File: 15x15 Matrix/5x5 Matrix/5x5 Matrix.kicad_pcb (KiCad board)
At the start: 2 copper layers, 111 parts, among them J1 Conn_01x02, SW1 SWP, SW10 SWP, SW11 SWP, SW12 SWP, SW13 SWP, SW14 SWP, SW15 SWP, SW16 SWP, SW17 SWP, SW18 SWP, SW19 SWP, SW2 SWP, SW20 SWP, SW21 SWP, SW22 SWP, SW23 SWP, SW24 SWP, SW25 SWP, SW3 SWP, SW4 SWP, SW5 SWP, SW6 SWP, SW7 SWP, SW8 SWP, SW9 SWP, U1 MCP23017-E/SO, U2 74AHCT1G125

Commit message: Added more pcb stuff
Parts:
- C1, C10, C11, C12, C13, C14, C15, C16, C17, C18, C19, C2, C20, C21, C22, C23, C24, C25, C27, C3, C4, C5, C6, C7, C8, C9, CPI1, CPI2, D26, D27, D28, D29, D30, D31, D32, D33, D34, D35, D36, D37, D38, D39, D40, D41, D42, D43, D44, D45, D46, D47, D48, D49, D50: moved to B.Cu
- moved D30 138.5 mm to (103.7, 40.1), turned to 180 degrees
- moved D31 126.4 mm to (103.7, 59.1), turned to 180 degrees
- moved D29 125.5 mm to (84.6, 40.1), turned to 180 degrees
- moved D28 114.4 mm to (65.6, 40.1), turned to 180 degrees
- moved D27 105.7 mm to (46.5, 40.1), turned to 180 degrees
- moved C1 102.0 mm to (27.6, 43.2), turned to 180 degrees
- moved D26 100.2 mm to (27.5, 40.1), turned to 180 degrees
- moved D48 31.0 mm to (24.9, 144.7), turned to 180 degrees
- moved D49 31.0 mm to (24.9, 149.3), turned to 180 degrees
- moved D50 31.0 mm to (24.9, 153.8), turned to 180 degrees
- moved D32 17.7 mm to (49.2, 167.5), turned to 180 degrees
- moved C25 17.2 mm to (60.6, 150.1), turned to 180 degrees
- moved CPI1 17.2 mm to (60.6, 155.4), turned to 180 degrees
- moved CPI2 17.2 mm to (60.6, 158.1), turned to 180 degrees
- moved C27 17.2 mm to (60.6, 152.7), turned to 180 degrees
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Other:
- board outline added: 3.2 x 2.8 mm

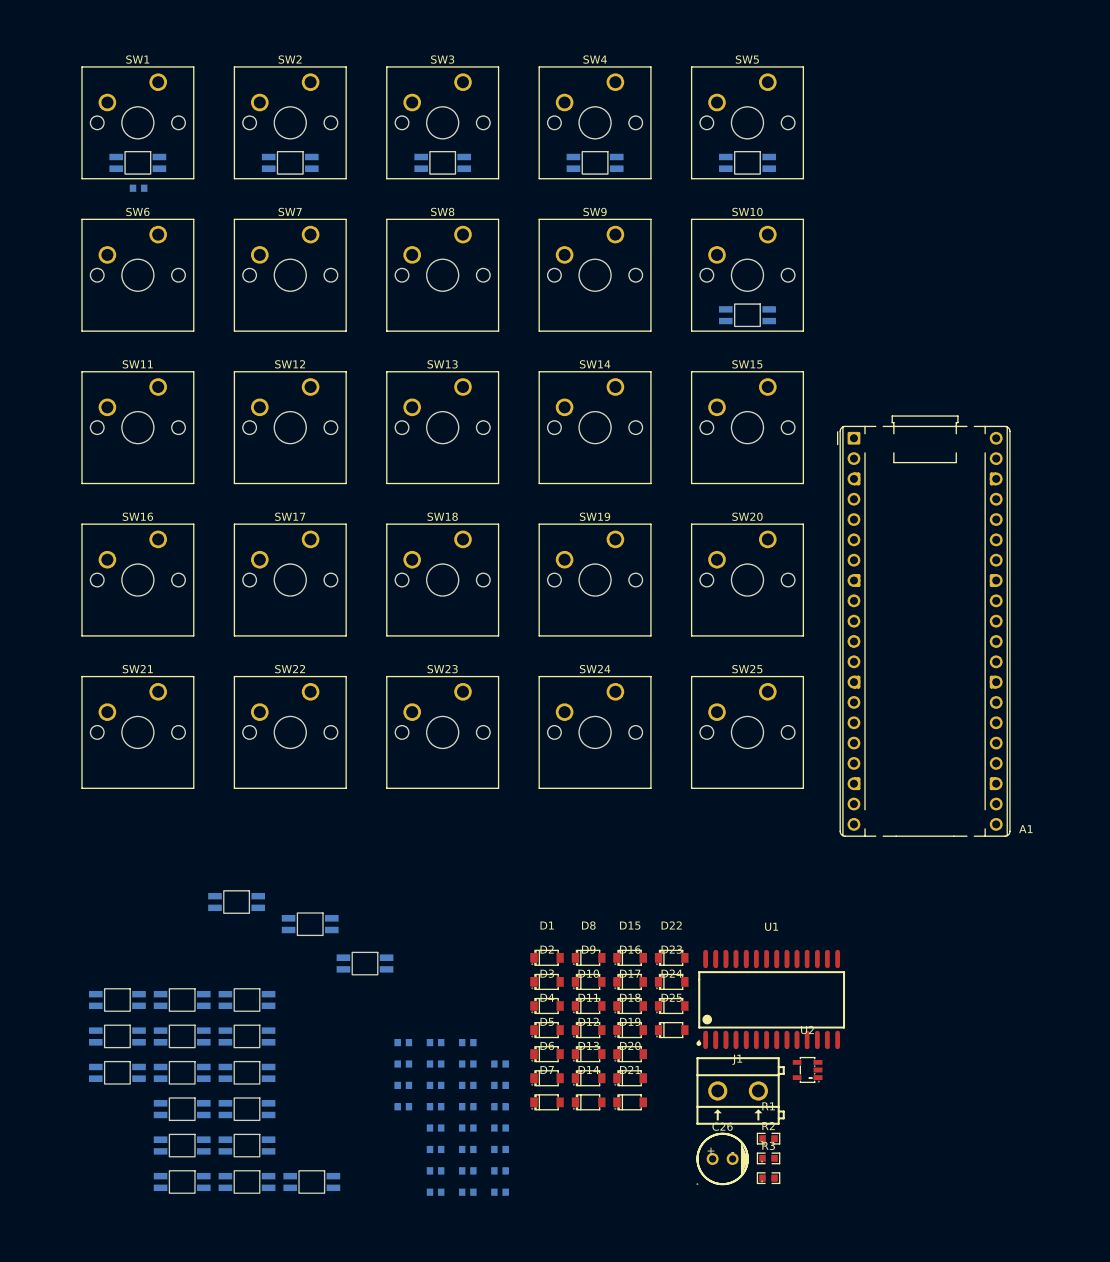
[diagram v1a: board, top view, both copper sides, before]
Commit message: Added led footprints
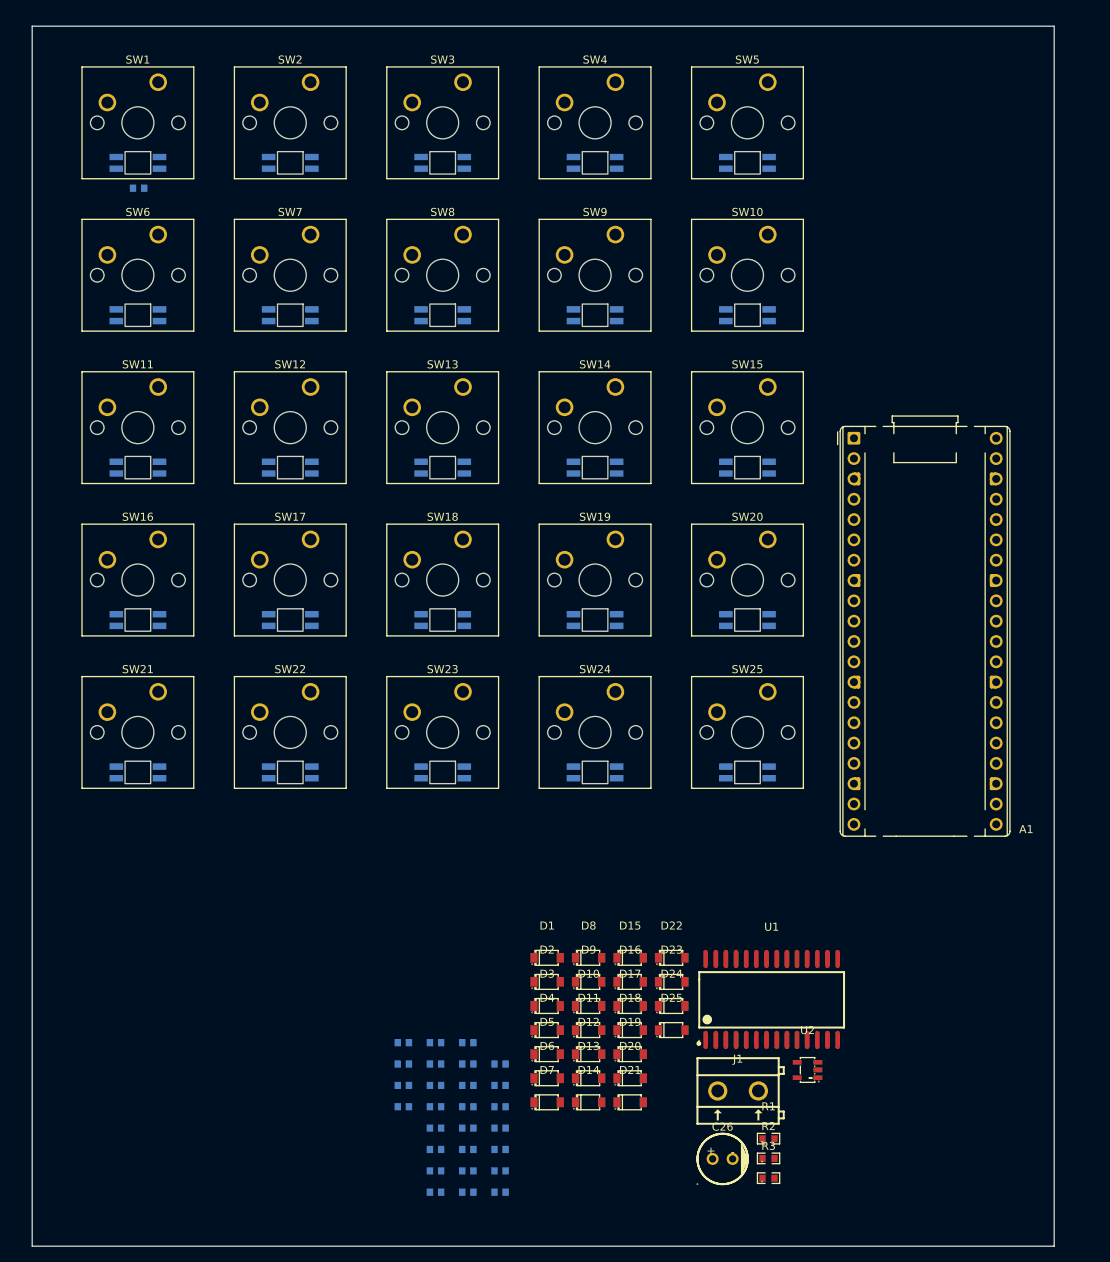
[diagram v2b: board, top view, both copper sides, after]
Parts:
- moved D32 114.0 mm to (84.6, 59.1)
- moved D39 99.3 mm to (84.6, 78.2)
- moved D35 91.2 mm to (27.5, 59.1)
- moved D38 88.2 mm to (65.6, 78.2)
- moved D50 87.3 mm to (103.7, 116.3)
- moved D34 85.8 mm to (46.5, 59.1)
- moved D41 85.1 mm to (103.7, 97.2)
- moved D37 80.4 mm to (46.5, 78.2)
- moved D40 79.0 mm to (103.7, 78.2)
- moved D33 77.7 mm to (65.6, 59.1)
- moved D36 76.9 mm to (27.5, 78.2)
- moved D42 73.3 mm to (84.6, 97.2)
- moved D49 68.2 mm to (84.6, 116.3)
- moved D45 65.9 mm to (27.5, 97.2)
- moved D43 65.3 mm to (65.6, 97.2)
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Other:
- board size 3.2 x 2.8 mm -> 127.8 x 152.5 mm
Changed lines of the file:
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@@
 	(footprint "footprints:C5149201_LED-SMD_4P-L3_2-W2_8-LS5_9_SK6812MINI-E"
 		(layer "B.Cu")
-		(at 33 167.475 180)
+		(at 27.46 116.28 180)
 		(property "Reference" "D46"
 			(at 0 4.725 0)
@@
 	(footprint "footprints:C5149201_LED-SMD_4P-L3_2-W2_8-LS5_9_SK6812MINI-E"
 		(layer "B.Cu")
-		(at 41.1 149.275 180)
+		(at 27.46 59.13 180)
 		(property "Reference" "D35"
 			(at 0 4.725 0)
@@
 	(footprint "footprints:C5149201_LED-SMD_4P-L3_2-W2_8-LS5_9_SK6812MINI-E"
 		(layer "B.Cu")
-		(at 24.9 153.825 180)
+		(at 103.66 116.28 180)
 		(property "Reference" "D50"
 			(at 0 4.725 0)
@@
 	(footprint "footprints:C5149201_LED-SMD_4P-L3_2-W2_8-LS5_9_SK6812MINI-E"
 		(layer "B.Cu")
-		(at 33 153.825 180)
+		(at 65.56 97.23 180)
 		(property "Reference" "D43"
 			(at 0 4.725 0)
@@
 	(footprint "footprints:C5149201_LED-SMD_4P-L3_2-W2_8-LS5_9_SK6812MINI-E"
 		(layer "B.Cu")
-		(at 33 158.375 180)
+		(at 46.51 97.23 180)
 		(property "Reference" "D44"
 			(at 0 4.725 0)
@@
 	(footprint "footprints:C5149201_LED-SMD_4P-L3_2-W2_8-LS5_9_SK6812MINI-E"
 		(layer "B.Cu")
-		(at 49.2 167.475 180)
+		(at 84.61 59.13 180)
 		(property "Reference" "D32"
 			(at 0 4.725 0)
@@
 	(footprint "footprints:C5149201_LED-SMD_4P-L3_2-W2_8-LS5_9_SK6812MINI-E"
 		(layer "B.Cu")
-		(at 39.8 132.48 180)
+		(at 65.56 59.13 180)
 		(property "Reference" "D33"
 			(at 0 4.725 0)
@@
 	(footprint "footprints:C5149201_LED-SMD_4P-L3_2-W2_8-LS5_9_SK6812MINI-E"
 		(layer "B.Cu")
-		(at 41.1 153.825 180)
+		(at 27.46 78.18 180)
 		(property "Reference" "D36"
 			(at 0 4.725 0)
@@
 	(footprint "footprints:C5149201_LED-SMD_4P-L3_2-W2_8-LS5_9_SK6812MINI-E"
 		(layer "B.Cu")
-		(at 33 149.275 180)
+		(at 84.61 97.23 180)
 		(property "Reference" "D42"
 			(at 0 4.725 0)
@@
 	(footprint "footprints:C5149201_LED-SMD_4P-L3_2-W2_8-LS5_9_SK6812MINI-E"
 		(layer "B.Cu")
-		(at 49 135.25 180)
+		(at 103.66 78.18 180)
 		(property "Reference" "D40"
 			(at 0 4.725 0)
@@
 	(footprint "footprints:C5149201_LED-SMD_4P-L3_2-W2_8-LS5_9_SK6812MINI-E"
 		(layer "B.Cu")
-		(at 41.1 144.725 180)
+		(at 46.51 59.13 180)
 		(property "Reference" "D34"
 			(at 0 4.725 0)
@@
 	(footprint "footprints:C5149201_LED-SMD_4P-L3_2-W2_8-LS5_9_SK6812MINI-E"
 		(layer "B.Cu")
-		(at 24.9 149.275 180)
+		(at 84.61 116.28 180)
 		(property "Reference" "D49"
 			(at 0 4.725 0)
@@
 	(footprint "footprints:C5149201_LED-SMD_4P-L3_2-W2_8-LS5_9_SK6812MINI-E"
 		(layer "B.Cu")
-		(at 41.1 158.375 180)
+		(at 46.51 78.18 180)
 		(property "Reference" "D37"
 			(at 0 4.725 0)
@@
 	(footprint "footprints:C5149201_LED-SMD_4P-L3_2-W2_8-LS5_9_SK6812MINI-E"
 		(layer "B.Cu")
-		(at 41.1 162.925 180)
+		(at 65.56 78.18 180)
 		(property "Reference" "D38"
 			(at 0 4.725 0)
@@
 	(footprint "footprints:C5149201_LED-SMD_4P-L3_2-W2_8-LS5_9_SK6812MINI-E"
 		(layer "B.Cu")
-		(at 33 162.925 180)
+		(at 27.46 97.23 180)
 		(property "Reference" "D45"
 			(at 0 4.725 0)
@@
 	(footprint "footprints:C5149201_LED-SMD_4P-L3_2-W2_8-LS5_9_SK6812MINI-E"
 		(layer "B.Cu")
-		(at 41.1 167.475 180)
+		(at 84.61 78.18 180)
 		(property "Reference" "D39"
 			(at 0 4.725 0)
@@
 	(footprint "footprints:C5149201_LED-SMD_4P-L3_2-W2_8-LS5_9_SK6812MINI-E"
 		(layer "B.Cu")
-		(at 33 144.725 180)
+		(at 103.66 97.23 180)
 		(property "Reference" "D41"
 			(at 0 4.725 0)
@@
 	(footprint "footprints:C5149201_LED-SMD_4P-L3_2-W2_8-LS5_9_SK6812MINI-E"
 		(layer "B.Cu")
-		(at 55.85 140.175 180)
+		(at 46.51 116.28 180)
 		(property "Reference" "D47"
 			(at 0 4.725 0)
@@
 	(footprint "footprints:C5149201_LED-SMD_4P-L3_2-W2_8-LS5_9_SK6812MINI-E"
 		(layer "B.Cu")
-		(at 24.9 144.725 180)
+		(at 65.56 116.28 180)
 		(property "Reference" "D48"
 			(at 0 4.725 0)
@@
 		)
 	)
+	(gr_rect
+		(start 14.25 23)
+		(end 142 175.5)
+		(stroke
+			(width 0.05)
+			(type default)
+		)
+		(fill no)
+		(layer "Edge.Cuts")
+	)
 	(embedded_fonts no)

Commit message: Fixed rotation of leds on pcb
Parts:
- turned D26 to 0 degrees
- turned D27 to 0 degrees
- turned D28 to 0 degrees
- turned D29 to 0 degrees
- turned D30 to 0 degrees
- turned D36 to 0 degrees
- turned D37 to 0 degrees
- turned D38 to 0 degrees
- turned D39 to 0 degrees
- turned D40 to 0 degrees
- turned D46 to 0 degrees
- turned D47 to 0 degrees
- turned D48 to 0 degrees
- turned D49 to 0 degrees
- turned D50 to 0 degrees

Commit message: 5x5 Ready for 1 sided printing
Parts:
- removed CPI1: 100nF, footprints:C14663_C0603
- C26: footprint footprints:C49304896_CAP-TH_BD6_3-P2_50-D0_5-FD -> Capacitor_THT:CP_Radial_D6.3mm_P2.50mm; moved to B.Cu
- D1, D10, D11, D12, D13, D14, D15, D16, D17, D18, D19, D2, D20, D21, D22, D23, D24, D25, D3, D4, D5, D6, D7, D8, D9, J1, R1, R2, R3, U1, U2: moved to B.Cu
- D26, D27, D28, D29, D30, D31, D32, D33, D34, D35, D36, D37, D38, D39, D40, D41, D42, D43, D44, D45, D46, D47, D48, D49, D50: footprint footprints:C5149201_LED-SMD_4P-L3_2-W2_8-LS5_9_SK6812MINI-E -> LED_SMD:LED_SK6812MINI-E_3.2x2.8mm_P1.5mm_ReverseMount
- moved R3 150.1 mm to (21.8, 43.0), turned to 180 degrees
- moved U2 145.0 mm to (15.8, 44.2), turned to 180 degrees
- moved D5 128.4 mm to (109.0, 26.8), turned to 180 degrees
- moved D4 122.3 mm to (89.9, 26.8), turned to 180 degrees
- moved D1 121.7 mm to (32.8, 26.8), turned to 180 degrees
- moved C5 121.7 mm to (103.7, 43.1)
- moved D3 119.0 mm to (70.8, 26.8), turned to 180 degrees
- moved D2 118.8 mm to (51.8, 26.8), turned to 180 degrees
- moved D6 118.0 mm to (32.8, 45.8), turned to 180 degrees
- moved C4 115.6 mm to (84.6, 43.1)
- moved D7 114.9 mm to (51.8, 45.8), turned to 180 degrees
- moved C27 114.5 mm to (15.4, 47.5), turned to 0 degrees
- moved C2 112.7 mm to (46.5, 43.1)
- moved C3 112.5 mm to (65.6, 43.1)
- moved C8 106.9 mm to (65.6, 62.1)
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- renumbered CPI2 to C28
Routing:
- net /5V: track 0.00 -> 727.9 mm
- net /ROW0: track 0.00 -> 260.6 mm, vias 0 -> 1
- net /3V3: track 0.00 -> 259.1 mm, vias 0 -> 3
- net /ROW1: track 0.00 -> 236.7 mm, vias 0 -> 1
- net /ROW2: track 0.00 -> 212.9 mm, vias 0 -> 1
- net /I2C_SDA: track 0.00 -> 205.6 mm, vias 0 -> 1
- net /I2C_SCL: track 0.00 -> 199.6 mm, vias 0 -> 1
- net /ROW3: track 0.00 -> 189.1 mm, vias 0 -> 1
- net /ROW4: track 0.00 -> 156.5 mm, vias 0 -> 1
- net /COL4: track 0.00 -> 156.1 mm
- net /COL0: track 0.00 -> 143.0 mm, vias 0 -> 6
- net /COL3: track 0.00 -> 138.0 mm, vias 0 -> 6
- net /GPIO2: track 0.00 -> 135.6 mm
- net /COL1: track 0.00 -> 122.5 mm, vias 0 -> 6
- net /COL2: track 0.00 -> 117.0 mm, vias 0 -> 6
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- added copper zone on B.Cu, net /GND
- added copper zone on F.Cu, net /GND
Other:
- board size 127.8 x 152.5 mm -> 134.8 x 132 mm
- board text added: "5V"
- board text added: "GND"

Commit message: Updated production files for single-sided
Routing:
- net /GND: track 50.4 -> 52.9 mm
